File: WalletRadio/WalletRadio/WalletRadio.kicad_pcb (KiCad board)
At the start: 2 copper layers, 105.9 x 64 mm, 30 parts, among them Q1001 Q_NMOS_DGS, Q1002 Q_NPN_ECB, SW1001 SW_DIP_x01, U1 LM324A

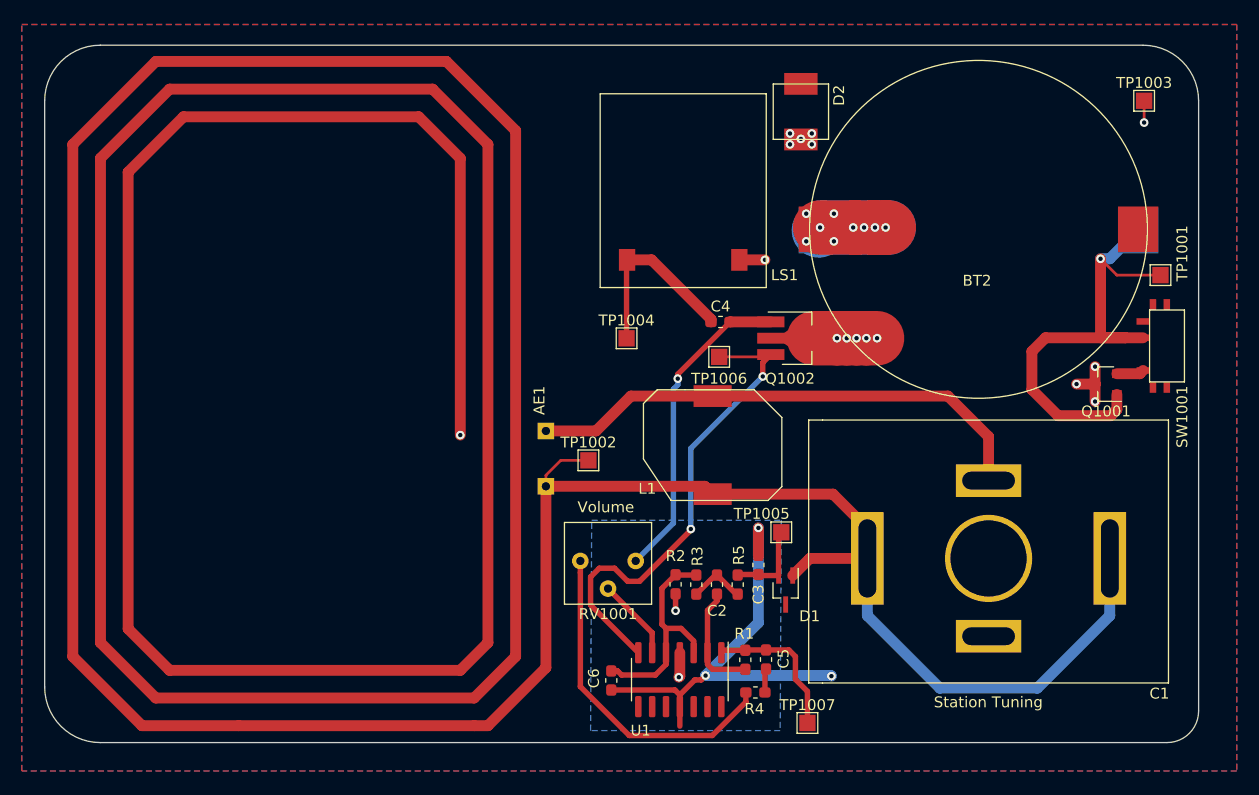
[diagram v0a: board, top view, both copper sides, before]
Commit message: Swapped out several parts and did some rerouting
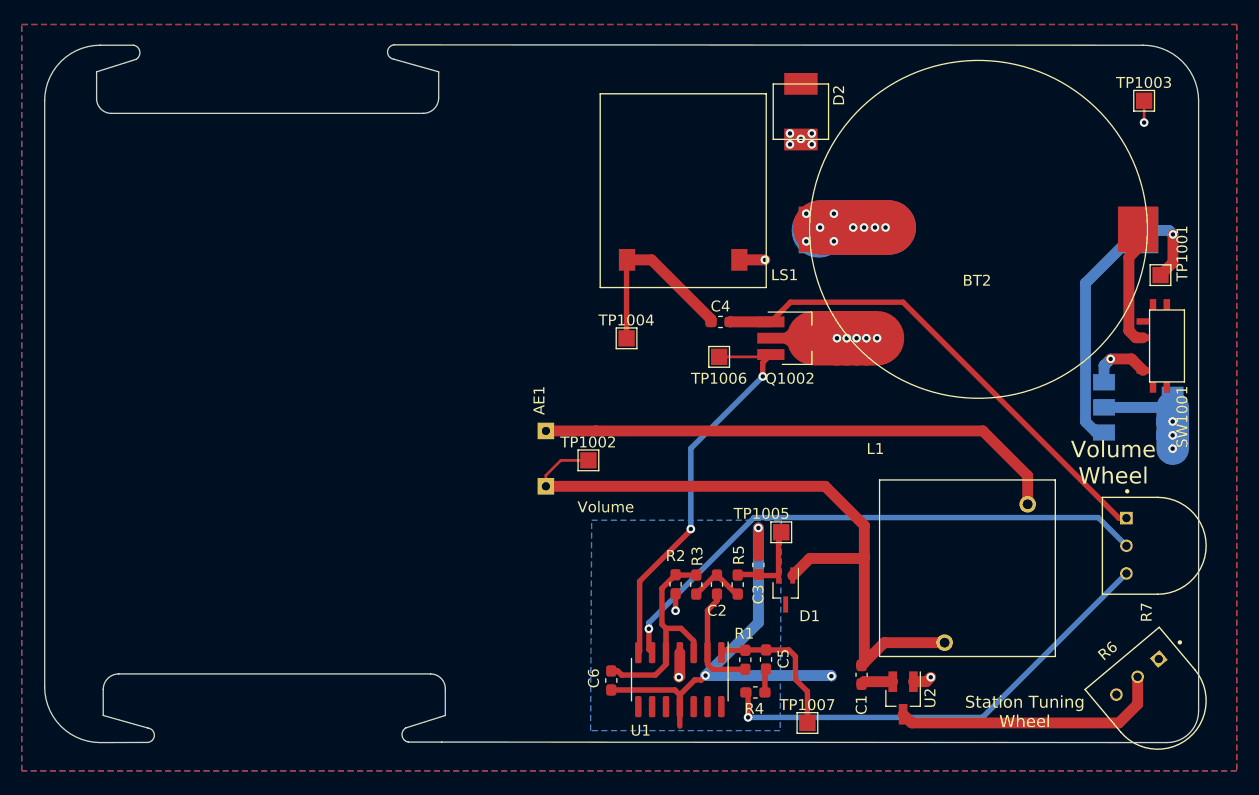
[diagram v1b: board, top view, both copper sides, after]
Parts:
- removed Q1001: Q_NMOS_DGS, Package_TO_SOT_SMD:SOT-23
- removed RV1001: 100K, WalletRadio:100Ohm_Pot
- added Q1: BSP315P, Package_TO_SOT_SMD:SOT-223, B.Cu at (204.5, 104.1)
- added R6: 3352T-1-103LF, WalletRadio:TRIM_3352T-1-103LF, F.Cu at (206.2, 131.1)
- added R7: 3352T-1-103LF, WalletRadio:TRIM_3352T-1-103LF, F.Cu at (206.2, 116.8)
- added U2: BB201, Package_TO_SOT_SMD:SOT-23_Handsoldering, F.Cu at (182.9, 130.8)
- C1: value 45-280pF -> 10n; footprint WalletRadio:464-PC_Trimmer -> Capacitor_SMD:C_0603_1608Metric_Pad1.08x0.95mm_HandSolder
- L1: value 320uH -> 168uH; footprint WalletRadio:7447714331_330uH -> WalletRadio:PE-53828NL
- moved L1 34.6 mm to (196.8, 121.9), turned to 180 degrees
- moved C1 15.8 mm to (179.1, 128.7), turned to 270 degrees
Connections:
- C1 pad 2: GND -> Net-(C1-Pad2)
- SW1001 pad 2: Net-(BT1-Pad1) -> GND
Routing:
- net Net-(AE1-Pad2): track 601.0 -> 64.9 mm, vias 1 -> 0
- net Net-(R7-Pad2): track 7.56 -> 51.8 mm, vias 0 -> 1
- net Net-(R6-Pad2): track 0.00 -> 25.1 mm
- net Net-(C4-Pad2): track 29.3 -> 45.3 mm, vias 1 -> 0
- net Net-(BT1-Pad1): track 44.8 -> 29.2 mm
- net GND: track 93.5 -> 106.0 mm, vias 4 -> 5
- net Net-(R4-Pad1): track 30.7 -> 42.6 mm, vias 0 -> 1
- net Net-(Q1002-Pad3): track 44.7 -> 37.2 mm
- net /+Vbat: track 16.5 -> 21.7 mm
- net Net-(Q1-Pad3): track 2.52 -> 5.80 mm, vias 0 -> 1
- net Net-(C1-Pad2): track 0.00 -> 2.96 mm
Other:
- outline, holes or cut-outs redrawn
- board text added: "Station Tuning Wheel"
- board text added: "Volume Wheel"
- board text removed: "Station Tuning"

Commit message: Changed to KiCad 6.0
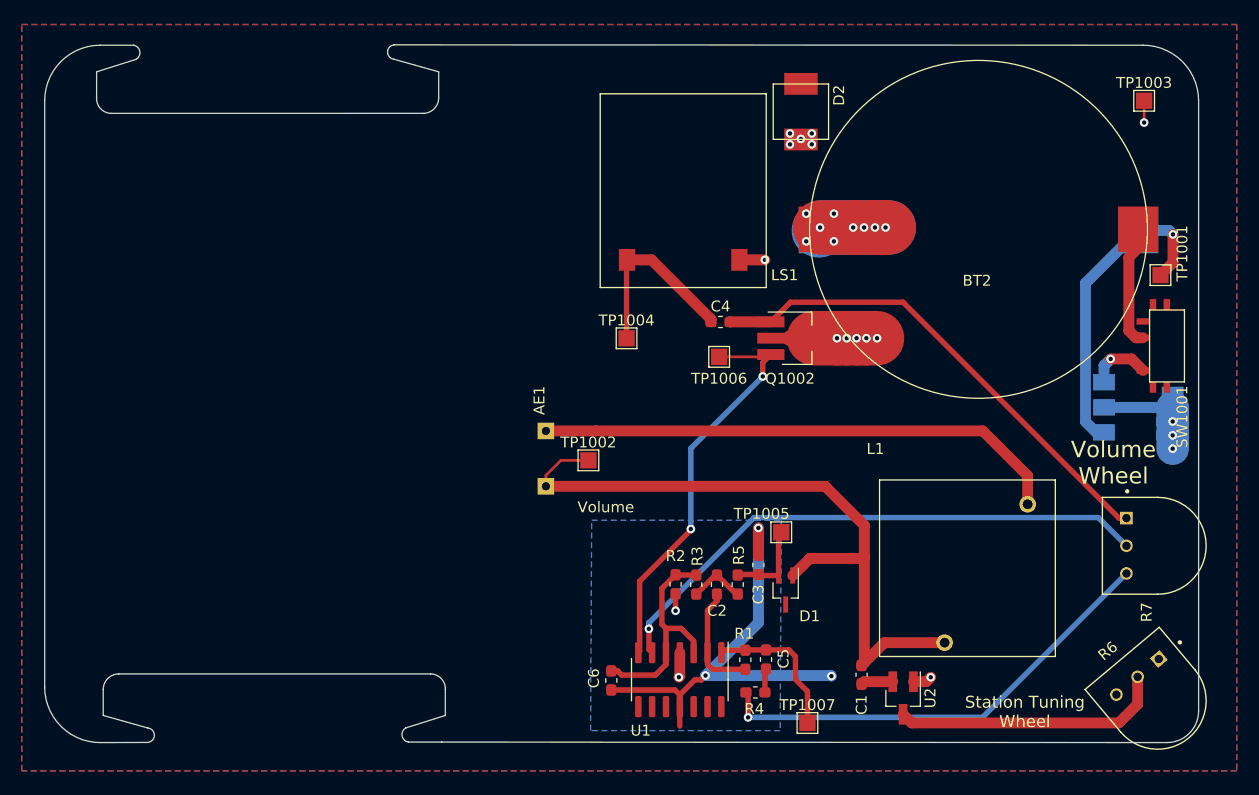
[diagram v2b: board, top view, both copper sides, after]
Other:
- net class Default removed

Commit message: Working on PCB antenna
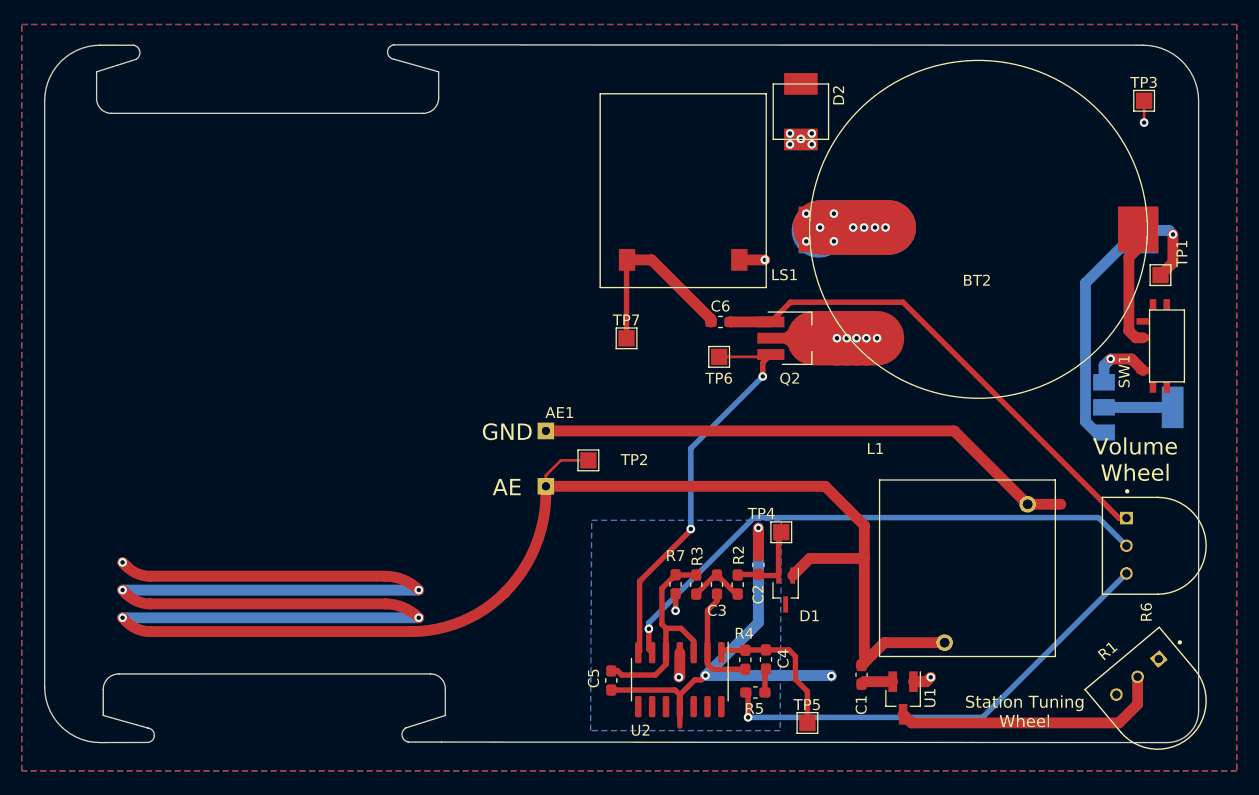
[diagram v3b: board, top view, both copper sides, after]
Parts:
- R6: renamed from R7; value 3352T-1-103LF -> 3352T-1-104LF
- renumbered C3 to C2, C2 to C3, C5 to C4, C6 to C5, C4 to C6, Q1002 to Q2, R6 to R1, R5 to R2, R1 to R4, R4 to R5, R2 to R7, SW1001 to SW1, TP1001 to TP1, TP1002 to TP2, TP1003 to TP3, TP1005 to TP4, TP1007 to TP5, TP1006 to TP6, TP1004 to TP7, U2 to U1, U1 to U2
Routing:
- net Net-(AE1-Pad2): track 64.9 -> 222.1 mm, vias 0 -> 5
- net /+Vbat: track 21.7 -> 17.9 mm, vias 16 -> 13
- net GND: track 106.0 -> 107.5 mm
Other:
- board text added: "AE"
- board text added: "GND"
- board text removed: "Volume"

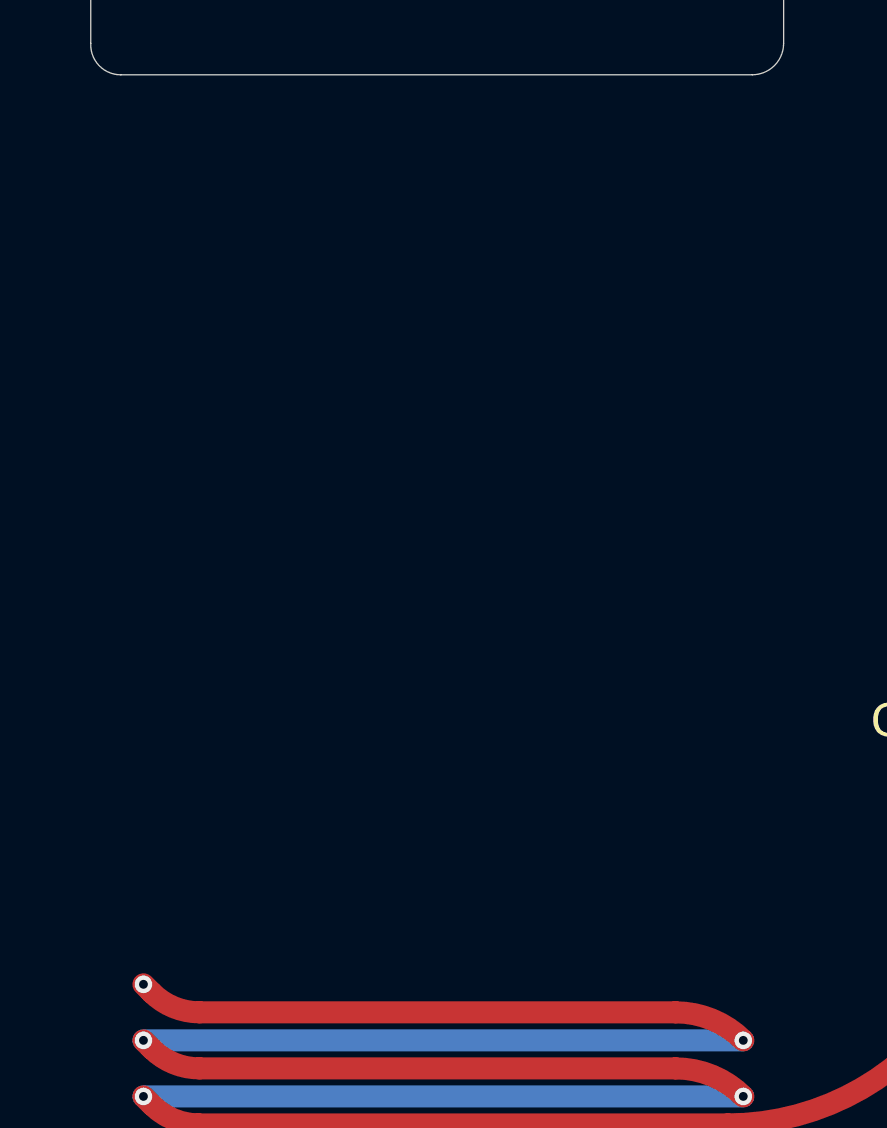
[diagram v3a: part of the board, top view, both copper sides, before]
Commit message: More embedded antenna work
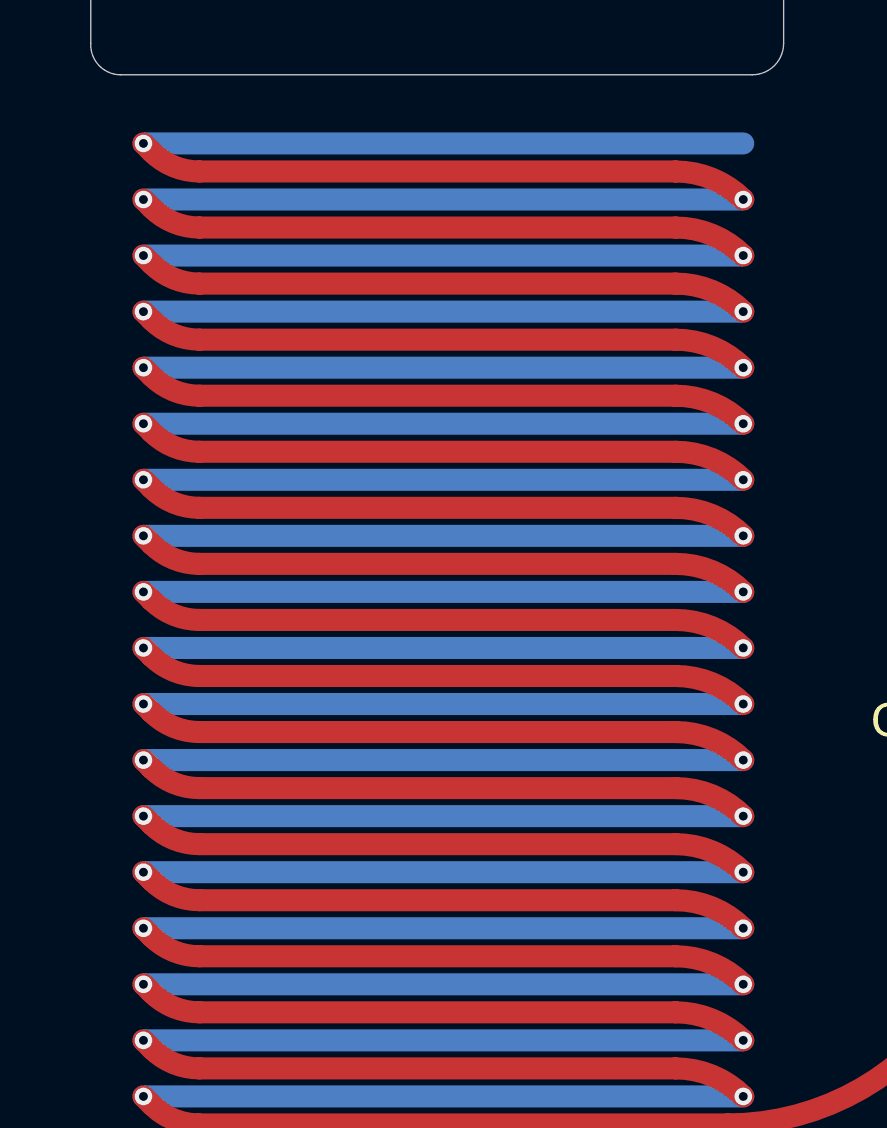
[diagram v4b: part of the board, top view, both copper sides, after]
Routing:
- net Net-(AE1-Pad2): track 222.1 -> 1075.0 mm, vias 5 -> 35

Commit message: Slight edits to PCB
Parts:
- added U2: BB201, Package_TO_SOT_SMD:SOT-23_Handsoldering, F.Cu at (180.3, 131.1)
- moved TP4 3.81 mm to (174.9, 113.5)
- moved TP2 3.07 mm to (153.4, 112.0)
- moved U1 2.79 mm to (185.7, 130.8)
- moved C1 2.45 mm to (179.3, 126.2)
- moved TP5 1.73 mm to (174.0, 131.4)
- renumbered U2 to U3
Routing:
- net Net-(AE1-Pad2): track 1075.0 -> 65.9 mm, vias 35 -> 0
- net GND: track 107.5 -> 61.3 mm, vias 5 -> 0
- net Net-(R1-Pad2): track 25.1 -> 33.1 mm, vias 0 -> 2
- net Net-(C1-Pad2): track 2.96 -> 7.27 mm
- net Net-(C2-Pad1): track 7.88 -> 11.9 mm
- net Net-(C4-Pad1): track 13.7 -> 10.7 mm
- net Net-(R6-Pad2): track 51.8 -> 49.4 mm
- net Net-(Q2-Pad3): track 37.2 -> 37.8 mm
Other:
- board text added: "+"
- board text added: "-"

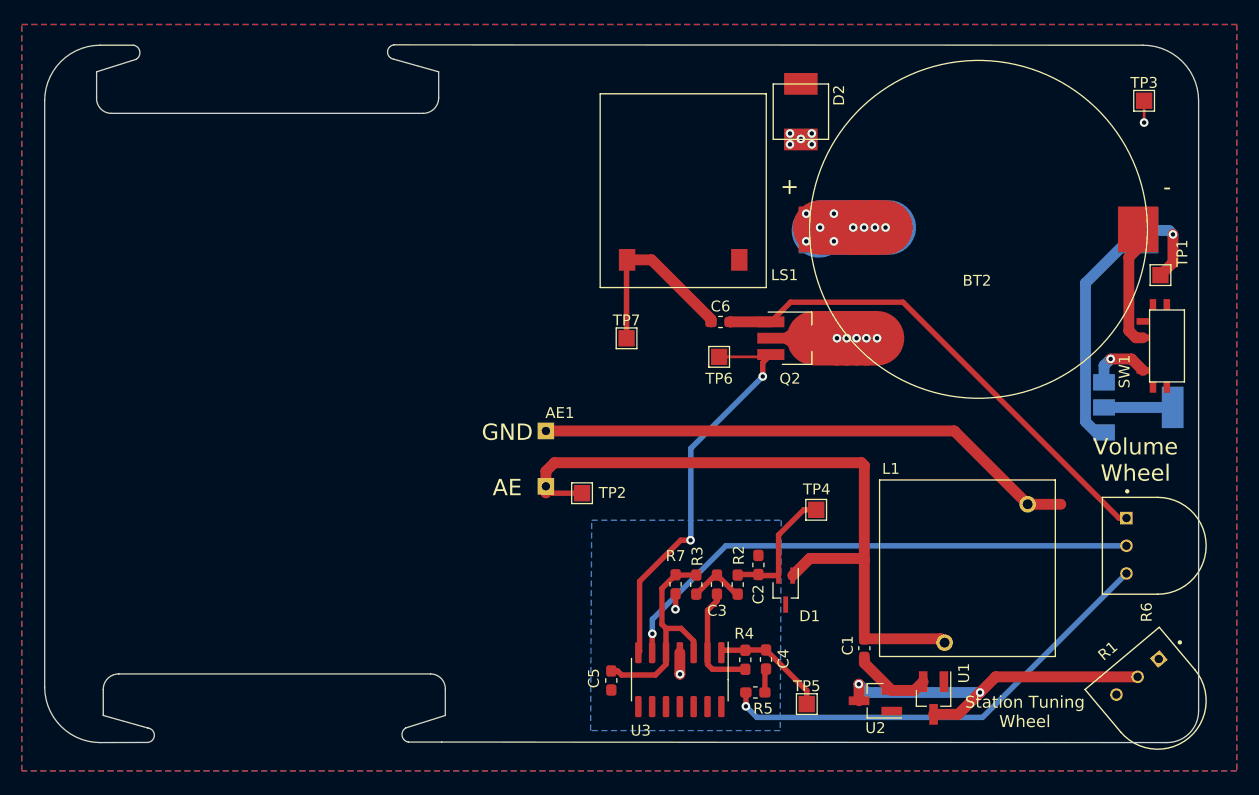
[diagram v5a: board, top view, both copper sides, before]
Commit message: Edited power switch, cleaned up layout
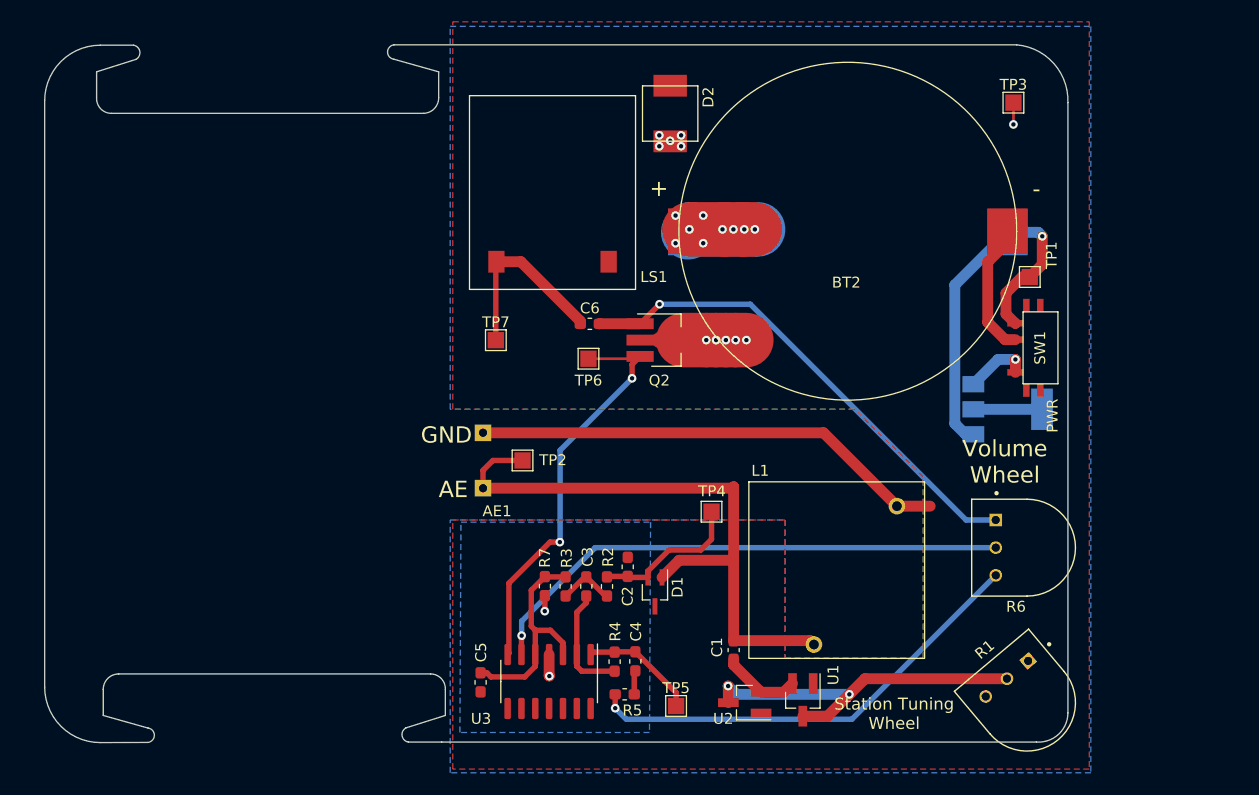
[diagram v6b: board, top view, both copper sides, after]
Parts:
- SW1: value SW_DIP_x01 -> SW_SPDT
- moved BT1 12.0 mm to (177.8, 88.1)
- moved BT2 12.0 mm to (177.8, 88.0)
- moved C1 12.0 mm to (167.3, 126.4)
- moved C2 12.0 mm to (157.6, 118.8)
- moved C3 12.0 mm to (153.8, 120.6)
- moved C4 12.0 mm to (158.3, 127.4)
- moved C5 12.0 mm to (144.1, 129.4)
- moved C6 12.0 mm to (154.1, 96.5)
- moved D1 12.0 mm to (160.1, 121.1)
- moved D2 12.0 mm to (161.5, 77.2)
- moved L1 12.0 mm to (184.9, 122.1)
- moved LS1 12.0 mm to (150.7, 90.8)
- moved Q1 12.0 mm to (192.5, 104.3)
- moved Q2 12.0 mm to (160.7, 98.0)
- moved R1 12.0 mm to (194.3, 131.2)
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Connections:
- SW1 pad 1: Net-(Q1-Pad3) -> GND
- SW1 pad 2: GND -> Net-(Q1-Pad3)
- SW1 pad 3: (no net) -> Net-(BT1-Pad1)
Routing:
- net Net-(AE1-Pad2): track 65.9 -> 57.8 mm
- net Net-(BT1-Pad1): track 29.2 -> 35.2 mm
- net GND: track 61.3 -> 56.1 mm
- net Net-(C2-Pad1): track 11.9 -> 14.0 mm
- net Net-(C6-Pad2): vias 0 -> 1
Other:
- board size 105.9 x 64 mm -> 93.9 x 64 mm
- board text added: "PWR"
